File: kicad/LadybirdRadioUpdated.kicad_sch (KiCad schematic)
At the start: 30 parts, among them Q1 BC547, Q2 BC337, Q3 BC337, T1 LT700

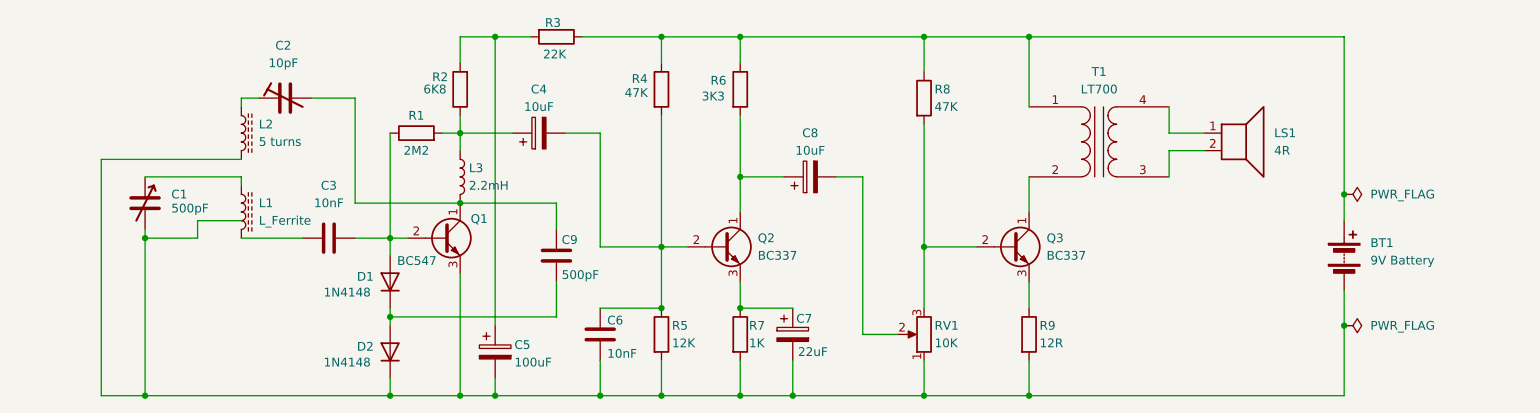
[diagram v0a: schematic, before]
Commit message: Added sockets and footprints
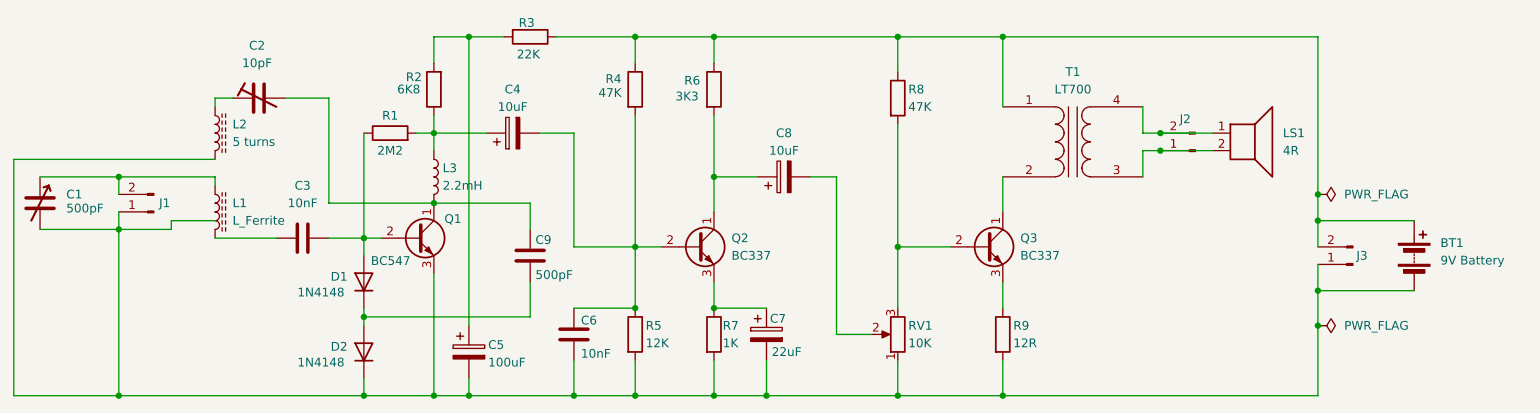
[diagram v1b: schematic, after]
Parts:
- added J1, J2, J3: Conn_01x02_Pin, Connector_Molex:Molex_KK-254_AE-6410-02A_1x02_P2.54mm_Vertical, symbol Connector:Conn_01x02_Pin
- C1, C3, C6, C9: footprint (none) -> Capacitor_THT:C_Rect_L7.2mm_W3.0mm_P5.00mm_FKS2_FKP2_MKS2_MKP2
- C2: footprint (none) -> Capacitor_SMD:C_Trimmer_Murata_TZB4-A
- C4, C5, C7, C8: footprint (none) -> Capacitor_THT:CP_Radial_D6.3mm_P2.50mm
- L1: footprint (none) -> Ferrite_THT:LairdTech_28C0236-0JW-10
- L3: footprint (none) -> Inductor_THT:Choke_EPCOS_B82722A
- R1, R2, R3, R4, R5, R6, R7, R8, R9, RV1: footprint (none) -> Resistor_THT:R_Axial_DIN0207_L6.3mm_D2.5mm_P10.16mm_Horizontal
- T1: footprint (none) -> ACRM:Transformer_LT722
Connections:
- net at BT1.2 (-), C1.2, C5.2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: now also J1.1 (Pin_1), J3.1 (Pin_1)
- net at BT1.1 (+), R3.1, R4.1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: now also J3.2 (Pin_2)
- net at LS1.2, T1.3 (SA): now also J2.1 (Pin_1)
- net at LS1.1, T1.4 (SB): now also J2.2 (Pin_2)
- net at C1.1, L1.1: now also J1.2 (Pin_2)
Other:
- moved on the sheet: BT1, C1, C2, C3, C4, C5, C6, C7, C8, C9, D1, D2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

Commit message: Initial board design
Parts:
- removed L1: L_Ferrite, Ferrite_THT:LairdTech_28C0236-0JW-10, symbol Device:L_Ferrite
- removed L2: 5 turns, symbol Device:L_Ferrite
- added J4: Conn_01x03_Pin, Connector_Molex:Molex_KK-254_AE-6410-03A_1x03_P2.54mm_Vertical, symbol Connector:Conn_01x03_Pin
- added L4: L_Ferrite_Dual_tapped_untapped, ACRM:FerriteRod_L76.2mm_D10.0mm Tapped_25mm Untapped 10mm, symbol ACRM:L_Ferrite_Dual_tapped_untapped
- L3: footprint Inductor_THT:Choke_EPCOS_B82722A -> Inductor_THT:L_Axial_L12.8mm_D5.8mm_P25.40mm_Horizontal_Fastron_HBCC
- Q1, Q2, Q3: footprint Package_TO_SOT_THT:TO-92_Inline -> Package_TO_SOT_THT:TO-92_HandSolder
- RV1: footprint Resistor_THT:R_Axial_DIN0207_L6.3mm_D2.5mm_P10.16mm_Horizontal -> (none)
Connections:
- net GND: now reaches BT1.2 (-), C1.2, C5.2, C6.2, C7.2, D2.1 (K), J1.1 (Pin_1), J3.1 (Pin_1), Q1.3 (E), R5.2, R7.2, R9.2, RV1.1
- net GND: now also J4.1 (Pin_1), L4.2, L4.4
- net at C1.1, J1.2 (Pin_2): now also L4.3
- net at C3.1: now also L4.1
- net at BT1.1 (+), J3.2 (Pin_2), R3.1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: now also T1.2 (AB); no longer T1.1 (AA)
- net at Q3.1 (C): now also T1.1 (AA); no longer T1.2 (AB)
- net at J2.1 (Pin_1), T1.3 (SA): now also LS1.1; no longer LS1.2
- net at J2.2 (Pin_2), T1.4 (SB): now also LS1.2; no longer LS1.1
- net at C2.1: now also L4.5
- net at C8.2, RV1.2: now also J4.2 (Pin_2)
- net at Q3.2 (B), R8.2, RV1.3: now also J4.3 (Pin_3)
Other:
- moved on the sheet: J2

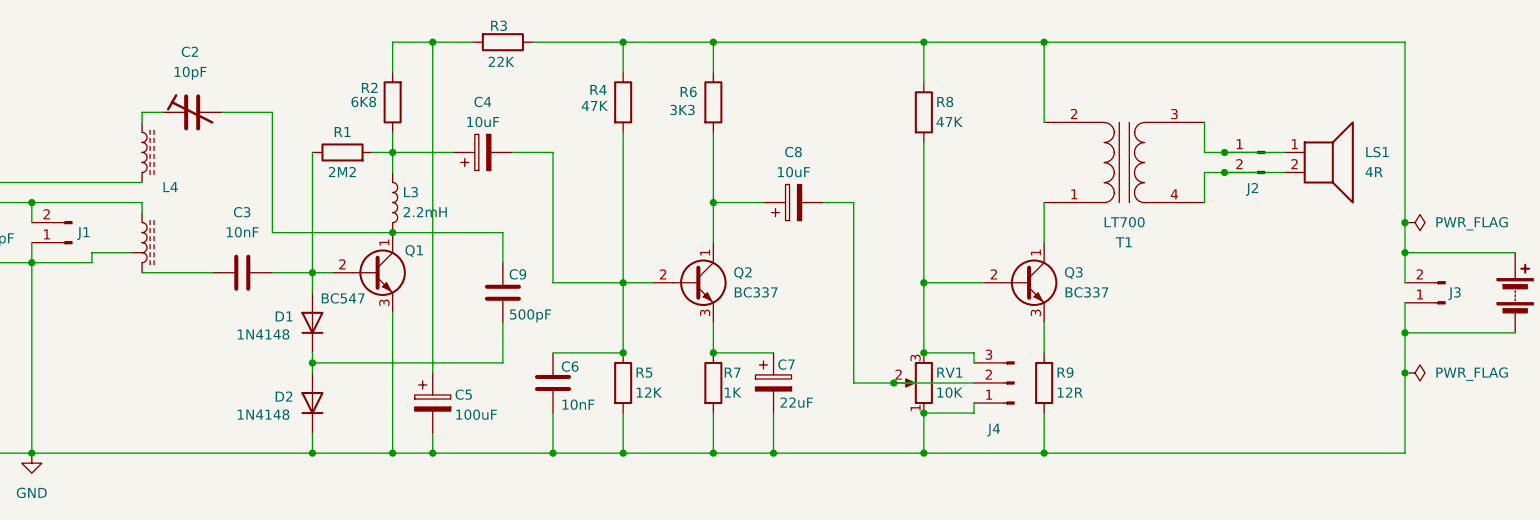
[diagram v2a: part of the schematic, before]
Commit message: Fixed transformer; Fixed temporary C-trimmer; Tidied ferrite; Tidied labels and values on silk screen
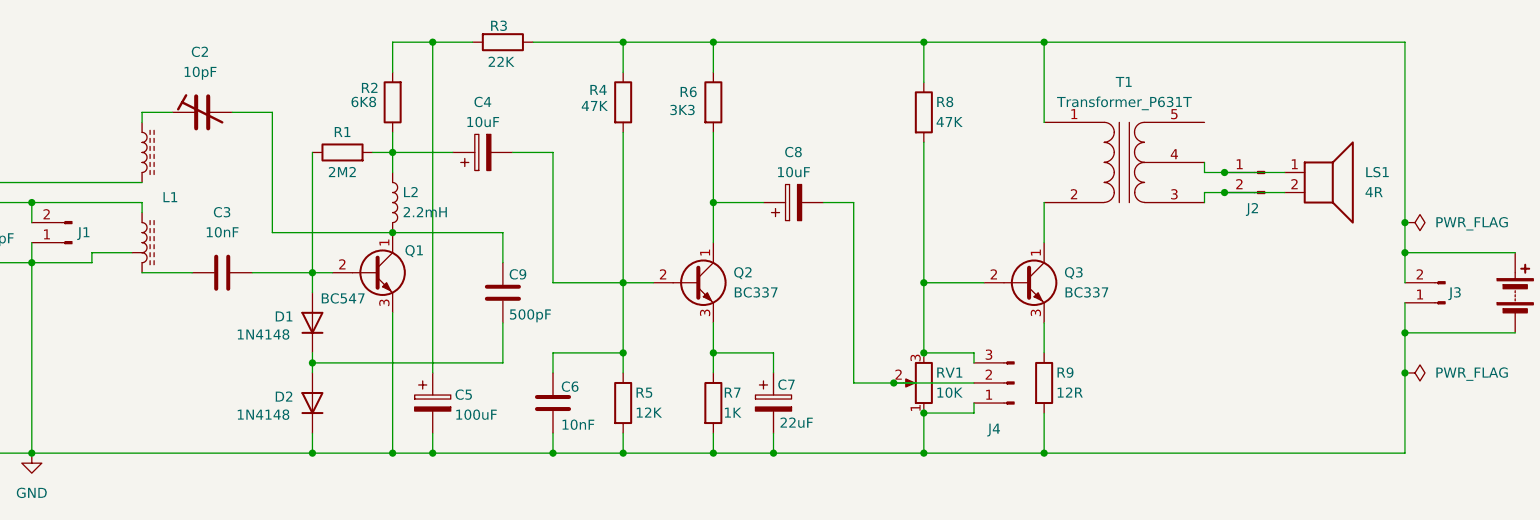
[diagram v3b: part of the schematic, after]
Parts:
- removed T1: LT700, ACRM:Transformer_LT722, symbol Device:Transformer_1P_1S
- added T1: Transformer_P631T, ACRM:Transformer_P631T, symbol ACRM:Transformer_P631T
- C2: footprint Capacitor_SMD:C_Trimmer_Murata_TZB4-A -> ACRM:C_Trimmer_THT
- renumbered L4 to L1, L3 to L2
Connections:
- net at Q3.1 (C): now also T1.2 (AB)
- net at BT1.1 (+), J3.2 (Pin_2), R3.1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: now also T1.1 (AA)
- net at J2.1 (Pin_1), LS1.1: now also T1.4 (SC)
- net at J2.2 (Pin_2), LS1.2: now also T1.3 (SA)
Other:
- moved on the sheet: C2, C3, C6, C7, J2, LS1, R5, R7

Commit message: Updated README
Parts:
- L2: footprint Inductor_THT:L_Axial_L12.8mm_D5.8mm_P25.40mm_Horizontal_Fastron_HBCC -> ACRM:L_Axial_L12.8mm_D5.8mm_P25.40mm_Horizontal_Radial_D9.5mm_P5.0mm
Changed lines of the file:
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@@
 			)
 		)
-		(property "Footprint" "Inductor_THT:L_Axial_L12.8mm_D5.8mm_P25.40mm_Horizontal_Fastron_HBCC"
+		(property "Footprint" "ACRM:L_Axial_L12.8mm_D5.8mm_P25.40mm_Horizontal_Radial_D9.5mm_P5.0mm"
 			(at 104.14 93.98 0)
 			(effects

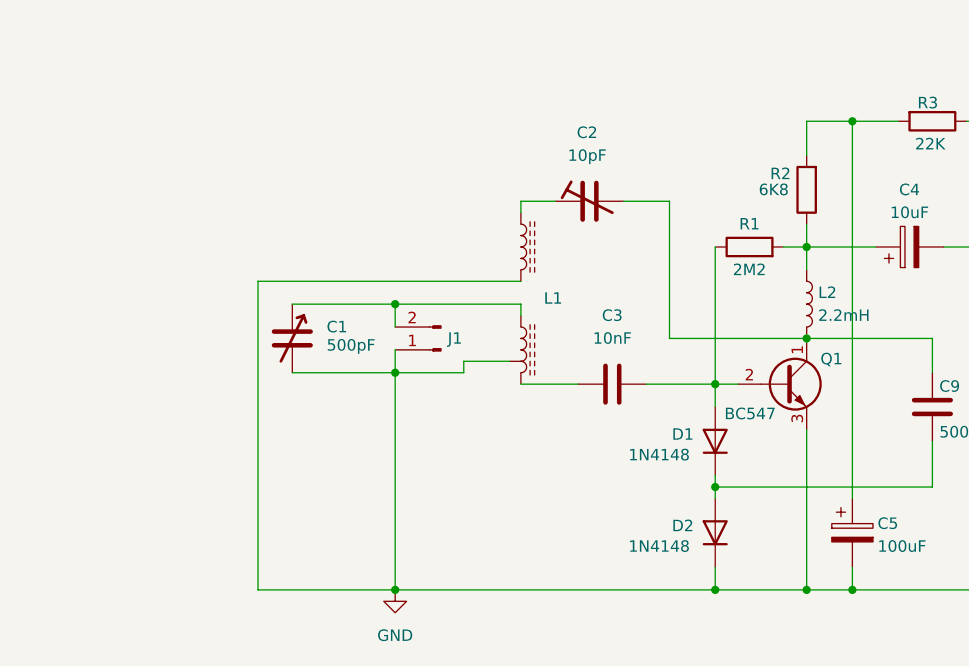
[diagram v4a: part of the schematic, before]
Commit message: Added options for crystal set
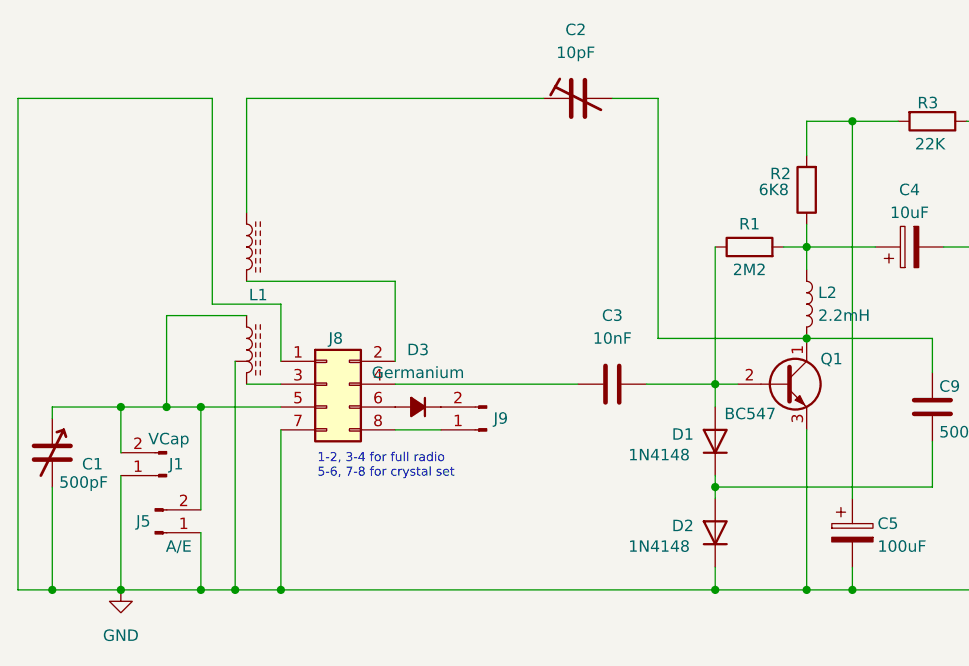
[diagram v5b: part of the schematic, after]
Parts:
- added D3: Germanium, Diode_THT:D_DO-41_SOD81_P10.16mm_Horizontal, symbol Device:D_Small_Filled
- added J5: A/E, Connector_Molex:Molex_KK-254_AE-6410-02A_1x02_P2.54mm_Vertical, symbol Connector:Conn_01x02_Pin
- added J8: Conn_02x04_Odd_Even, Connector_PinHeader_2.54mm:PinHeader_2x04_P2.54mm_Vertical, symbol Connector_Generic:Conn_02x04_Odd_Even
- added J9: Conn_01x02_Pin, Connector_Molex:Molex_KK-254_AE-6410-02A_1x02_P2.54mm_Vertical, symbol Connector:Conn_01x02_Pin
- J1: value Conn_01x02_Pin -> VCap
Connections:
- net GND: now also J5.1 (Pin_1), J8.1 (Pin_1), J8.7 (Pin_7); no longer L1.4
- net at C1.1, J1.2 (Pin_2), L1.3: now also J5.2 (Pin_2), J8.5 (Pin_5)
- net at C3.1: now also J8.4 (Pin_4); no longer L1.1
- new net: D3.1 (K), J9.2 (Pin_2)
- new net: D3.2 (A), J8.6 (Pin_6)
- new net: J8.2 (Pin_2), L1.4
- new net: J8.3 (Pin_3), L1.1
- new net: J8.8 (Pin_8), J9.1 (Pin_1)
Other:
- note added: "1-2, 3-4 for full radio 5-6, 7-8 for crystal set"
- moved on the sheet: C1, C2, J1, L1

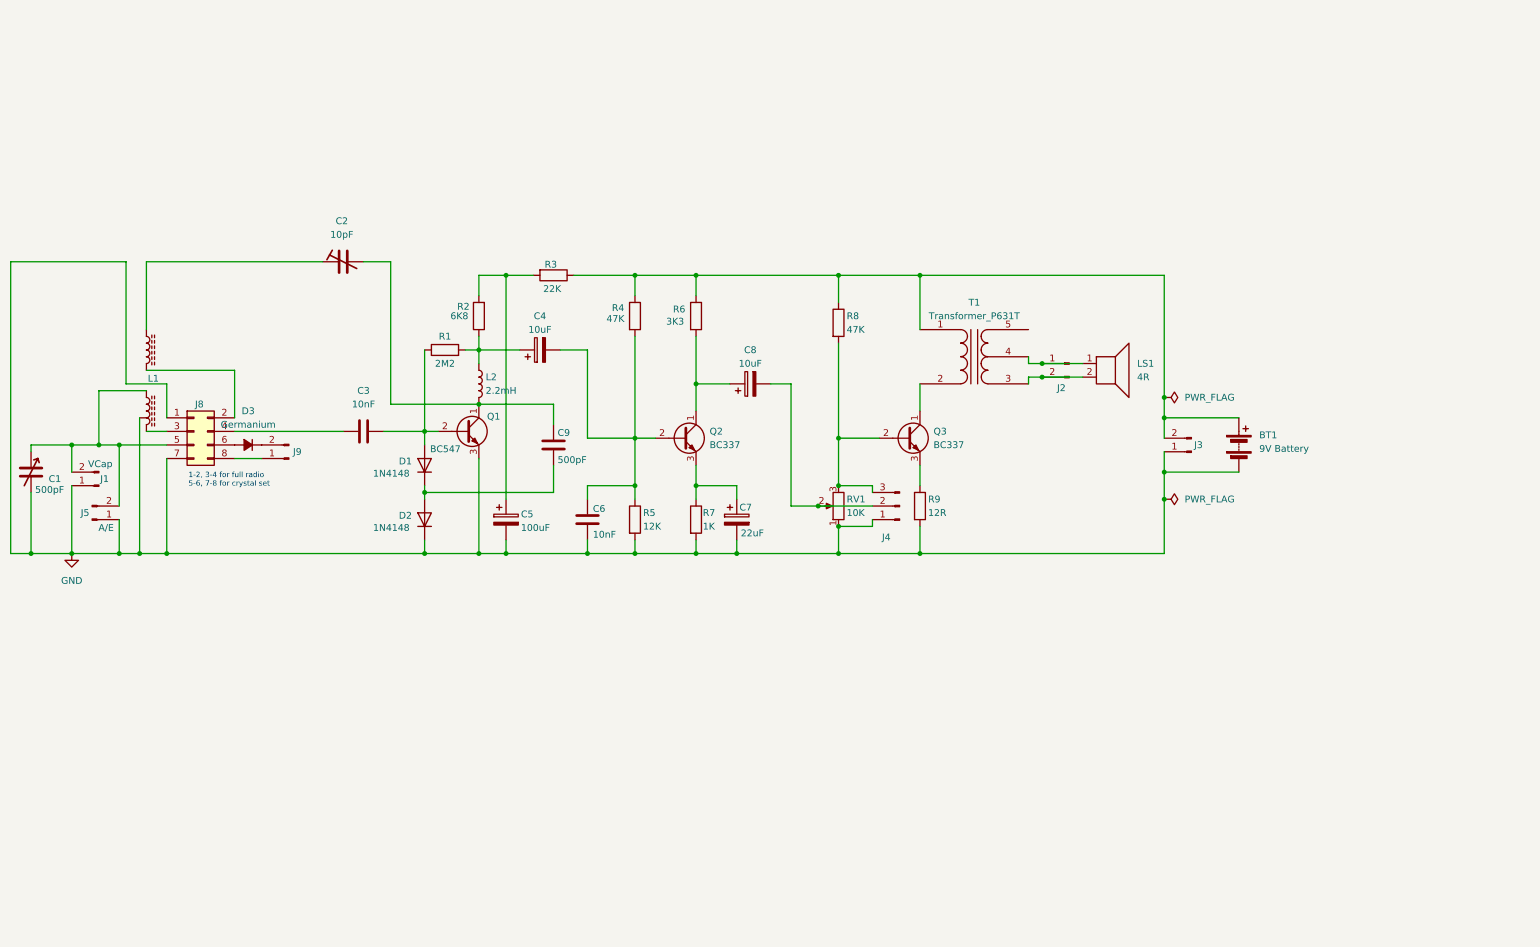
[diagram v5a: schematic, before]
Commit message: Separated out so this is just Crystal and Onetransistor
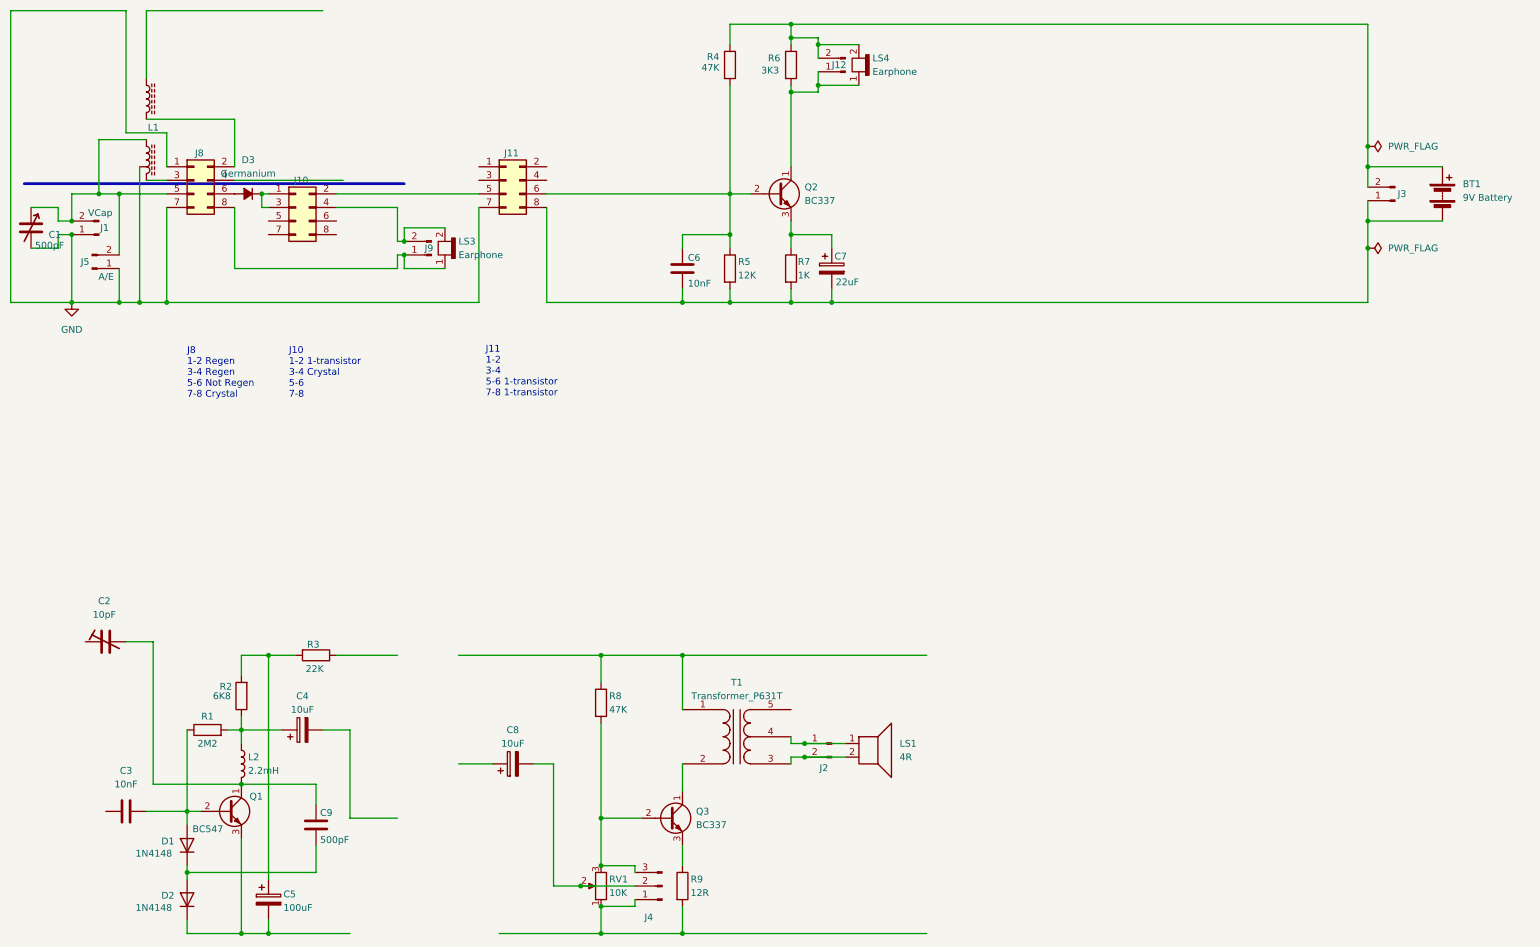
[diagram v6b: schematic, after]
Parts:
- added J10, J11: Conn_02x04_Odd_Even, Connector_PinHeader_2.54mm:PinHeader_2x04_P2.54mm_Vertical, symbol Connector_Generic:Conn_02x04_Odd_Even
- added J12: Conn_01x02_Pin, Connector_Molex:Molex_KK-254_AE-6410-02A_1x02_P2.54mm_Vertical, symbol Connector:Conn_01x02_Pin
- added LS3, LS4: Earphone, symbol Device:Earphone
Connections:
- net GND: now also J11.7 (Pin_7); no longer BT1.2 (-), C5.2, C6.2, C7.2, D2.1 (K), J3.1 (Pin_1), J4.1 (Pin_1), Q1.3 (E), R5.2, R7.2, R9.2, RV1.1
- net at BT1.1 (+), J3.2 (Pin_2), R4.1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: now also J12.2 (Pin_2), LS4.2 (+); no longer R3.1, R8.1, T1.1 (AA)
- net at C3.1: no longer J8.4 (Pin_4)
- net at C6.1, Q2.2 (B), R4.2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: now also J11.6 (Pin_6); no longer C4.2
- net at D3.1 (K): now also J10.1 (Pin_1), J10.3 (Pin_3); no longer J9.2 (Pin_2)
- net at J8.8 (Pin_8), J9.1 (Pin_1): now also LS3.1 (-)
- net at Q2.1 (C), R6.2: now also J12.1 (Pin_1), LS4.1 (-); no longer C8.1
- net at C2.1: no longer L1.5
- new net: R8.1, T1.1 (AA)
- new net: BT1.2 (-), C6.2, C7.2, J11.8 (Pin_8), J3.1 (Pin_1), R5.2, R7.2
- new net: C5.2, D2.1 (K), Q1.3 (E)
- new net: J4.1 (Pin_1), R9.2, RV1.1
- new net: J10.2 (Pin_2), J11.5 (Pin_5)
- new net: J10.4 (Pin_4), J9.2 (Pin_2), LS3.2 (+)
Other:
- note added: "J10 1-2 1-transistor 3-4 Crystal 5-6 7-8"
- note added: "J11 1-2 3-4 5-6 1-transistor 7-8 1-transistor"
- note added: "J8 1-2 Regen 3-4 Regen 5-6 Not Regen 7-8 Crystal"
- note removed: "1-2, 3-4 for full radio 5-6, 7-8 for crystal set"
- moved on the sheet: BT1, C1, C2, C3, C4, C5, C6, C7, C8, C9, D1, D2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
